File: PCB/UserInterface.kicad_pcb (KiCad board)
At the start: 2 copper layers, 8 parts, among them J10 B2B-PH-K-S, J11 B2B-PH-K-S, J2 Conn_01x12, J3 Conn_01x16, J9 B3B-PH-K-S

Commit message: Add files via upload
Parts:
- added REF**: MountingHole_2.7mm_M2.5_ISO7380, MountingHole:MountingHole_2.7mm_M2.5_ISO7380, F.Cu at (73.7, 139.2)
- added REF**: MountingHole_2.7mm_M2.5_ISO7380, MountingHole:MountingHole_2.7mm_M2.5_ISO7380, F.Cu at (173.7, 138.7)
- added REF**: MountingHole_2.7mm_M2.5_ISO7380, MountingHole:MountingHole_2.7mm_M2.5_ISO7380, F.Cu at (173.7, 114.8)
- added REF**: MountingHole_2.7mm_M2.5_ISO7380, MountingHole:MountingHole_2.7mm_M2.5_ISO7380, F.Cu at (74.7, 115.3)
- moved DPSext1 15.1 mm to (155.5, 137.7)
- moved MainBoard1 11.2 mm to (158.5, 120.9)
- moved J10 10.3 mm to (86.9, 128.5)
- moved J11 10.3 mm to (79.2, 128.6)
- moved S1 10.2 mm to (82.8, 137.2)
- moved J9 10.1 mm to (145.8, 120.9)
- moved J3 9.20 mm to (99.6, 137.2)
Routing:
- net /3V3: track 0.00 -> 71.5 mm
- net /OLEDBUTA: track 0.00 -> 18.2 mm
- net /DPSMOSI: track 0.00 -> 18.0 mm
- net /DPSMISO: track 0.00 -> 18.0 mm
- net /DPSCLK: track 0.00 -> 18.0 mm
- net /CS2: track 0.00 -> 18.0 mm
- net /OLEDSCL: track 0.00 -> 12.6 mm
- net /OLEDSDA: track 0.00 -> 12.1 mm
- net Net-(J11-Pad1): track 0.00 -> 10.0 mm
- net Net-(J10-Pad1): track 0.00 -> 9.17 mm
- added copper zone on B.Cu, net GND
- added copper zone on F.Cu, net GND
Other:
- board outline added: 106.7 x 30.5 mm

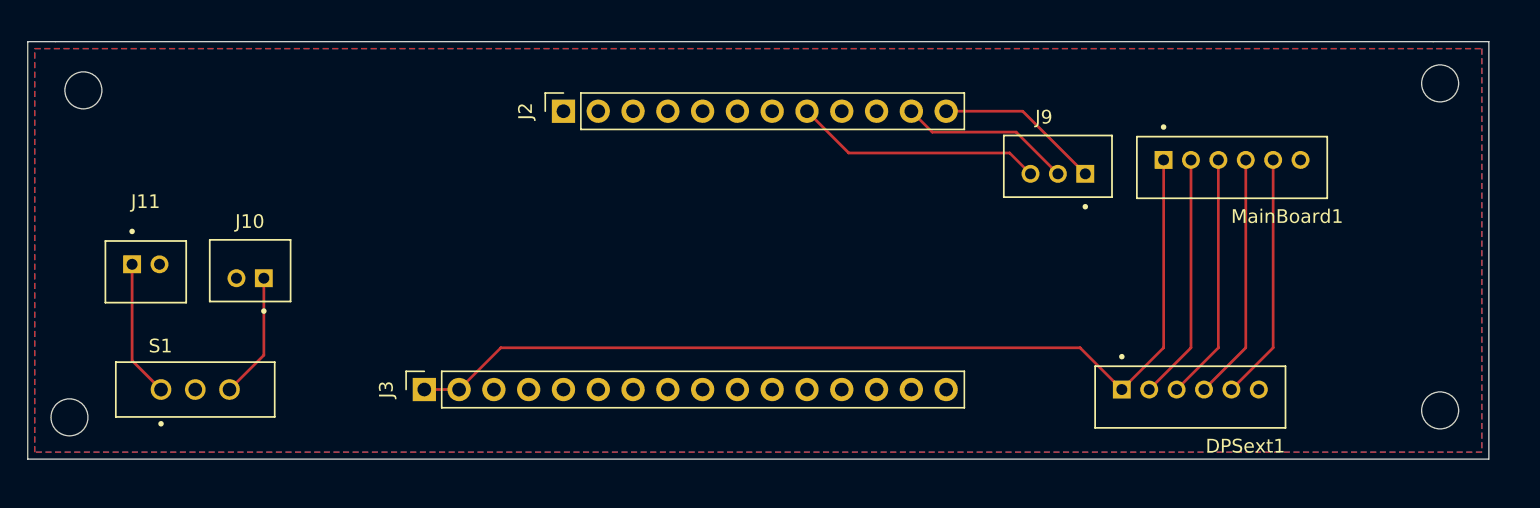
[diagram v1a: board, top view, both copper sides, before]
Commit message: Add files via upload
Updated Sizing on User Interface
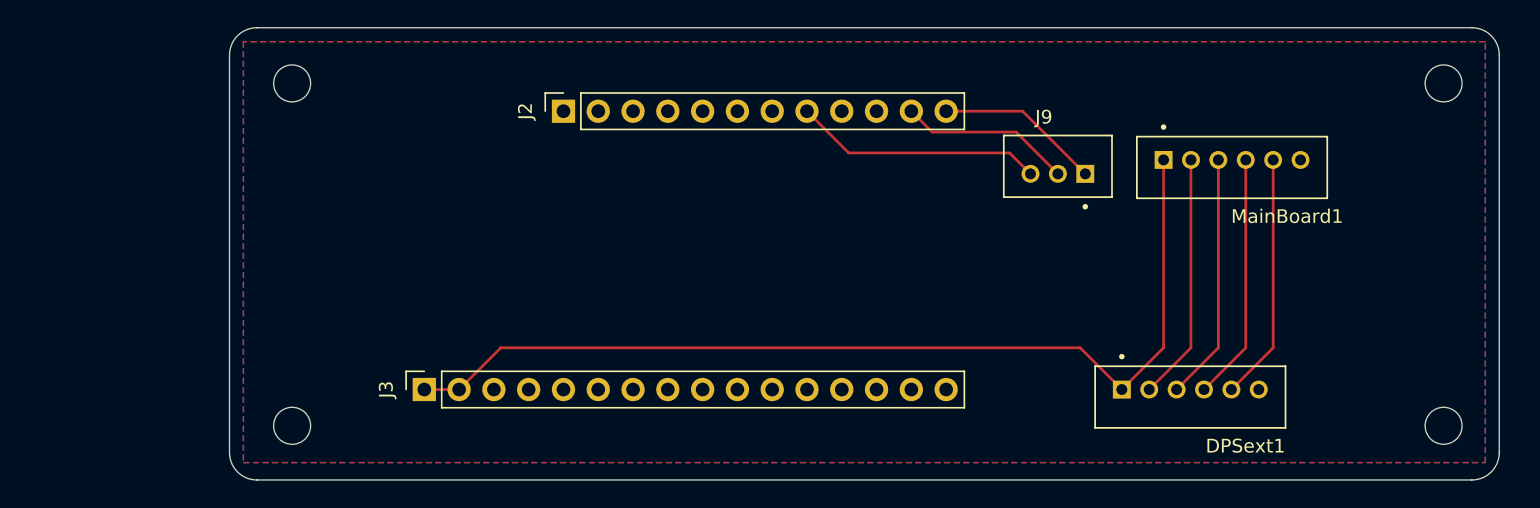
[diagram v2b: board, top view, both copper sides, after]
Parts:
- removed J10, J11: B2B-PH-K-S, B2B_PH_K_S:JST_B2B-PH-K-S
- removed S1: EG1218, EG1218:SW_EG1218
- moved REF** 16.3 mm to (89.9, 139.8)
- moved REF** 15.2 mm to (89.9, 114.8)
- moved REF** 1.15 mm to (174.0, 139.8)
- moved REF** 0.25 mm to (174.0, 114.8)
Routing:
- net Net-(J11-Pad1): track 10.0 -> 0.00 mm
- net Net-(J10-Pad1): track 9.17 -> 0.00 mm
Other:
- board size 106.7 x 30.5 mm -> 92.7 x 33 mm
